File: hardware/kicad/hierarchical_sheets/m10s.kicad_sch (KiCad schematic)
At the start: 0 parts

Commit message: massive comment upload
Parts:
- added U7: MAX-M10S, RF_GPS:ublox_MAX, symbol RF_GPS:MAX-M10S
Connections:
- new net: U7.1 (GND), U7.10 (GND), U7.12 (GND)
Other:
- note added: "Comments: - The I2C address is 0x42 (pg 15 in datasheet). Put something like "Addr: 0x42" in a text label near the bottom right of the chip so we know for future reference. - Since we are using I2C, we do not need the UART pins. Mark RXD and TXD as no connect - RF_IN: This is the main antenna connection, connect it to the SMA connector that is in the parts library under the name "CONSMA020.062-G"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"
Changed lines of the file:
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@@
     (company "Missouri S&T Rocket Design Team")
   )
+  (text "Comments:\n\n- The I2C address is 0x42 (pg 15 in datasheet). Put something like \"Addr: 0x42\" in a text label near the bottom right\n	of the chip so we know for future reference. \n\n- Since we are using I2C, we do not need the UART pins. Mark RXD and TXD as no connect\n\n- RF_IN: This is the main antenna connection, connect it to the SMA connector that is in the parts library under the\n	 name \"CONSMA020.062-G\". Pin 2 of that sma connector is the shield and should just go to ground. \n\n- Page 11 of the daatasheet: both VCC and VCC_IO are the supply pins. Connect both of these to 3.3v. Since they are the main supply\n	pins put two 100n capacitors on the schematic between 3.3v and gnd. These are decoupling capacitors that need to be placed \n	near the chip on the pcb. To help us remember, place them physically close to the vcc pins on the schematic. Check the \n	microcontroller schematic for an example.\n\n- On page 28 of the M10s integration manual (I just added this to datasheets), it says to leave the V_BCKP pin disconnected \n	if a backup supply is not used. Thus put a no connect on the V_BCKP pin. \n\n- On page 6 of the M10s integration manual, it says that VCC_RF is an optional voltage output for powering an optional external\n	LNA or active antenna. Since we are using a passive antenna just put a no connect on the VCC_RF pin. \n\n- Since there is no external LNA mark the LNA_EN as disabled\n\n- The Timepulse pin can be used to output a very precise time signal (gps atomic clock precision). We don't need it so just \n	mark it as no connect\n\n- The ExtInt pin is a configurable interrupt. We don't really have the need or pins for this so just mark it as no connect. \n\n- SDA and SCL are the I2C data lines, connect them to hierarchical labels so that we can connect them to the microcontroller\n	outside this schematic\n\n- The safeboot pin is used for flashing the chip firmware. We do not need to do this (hopefully) so just mark it as no connect.\n	\n- The VIO_SEL selects the I/O voltage for the module. According to page 9 of the datasheet, this pin should be left open (unconnected)\n	for 3.3v logic levels. As such, mark this pin as no connect. \n\n- NOTE!!!: We need to check the max10s footprint, i briefly looked at it and i\n	thought all the pins were reveresed when comparing it to the datasheet.\n	Unsure if datasheet is not clear or if the kicad footprint is backwards\n\n			-Seth"
+    (at 179.705 161.925 0)
+    (effects (font (size 2 2) (thickness 0.4) bold (color 255 48 0 1)) (justify left bottom))
+  )
+  (symbol (lib_id "RF_GPS:MAX-M10S") (at 95.885 93.345 0) (unit 1)
+    (in_bom yes) (on_board yes) (dnp no) (fields_autoplaced)
+    (property "Reference" "U7" (at 98.0791 110.49 0)
+      (effects (font (size 1.27 1.27)) (justify left))
+    )
+    (property "Value" "MAX-M10S" (at 98.0791 113.03 0)
+      (effects (font (size 1.27 1.27)) (justify left))
+    )
+    (property "Footprint" "RF_GPS:ublox_MAX" (at 106.045 109.855 0)
+      (effects (font (size 1.27 1.27)) hide)
+    )
+    (property "Datasheet" "https://content.u-blox.com/sites/default/files/MAX-M10S_DataSheet_UBX-20035208.pdf" (at 95.885 93.345 0)
+      (effects (font (size 1.27 1.27)) hide)
+    )
+    (pin "1")
+    (pin "10")
+    (pin "11")
+    (pin "12")
+    (pin "13")
+    (pin "14")
+    (pin "15")
+    (pin "16")
+    (pin "17")
+    (pin "18")
+    (pin "2")
+    (pin "3")
+    (pin "4")
+    (pin "5")
+    (pin "6")
+    (pin "7")
+    (pin "8")
+    (pin "9")
+    (instances
+      (project "FC"
+        (path "/54cce219-8b98-4e71-96c4-f9ee784aa3bc/f2d155c9-a158-4cf0-b4ab-42b0987153ce"
+          (reference "U7") (unit 1)
+        )
+      )
+    )
+  )
 )

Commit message: made gps
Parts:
- added C1, C2: 100n, symbol Device:C_Small
- added J5: CONSMA020.062-G, CONSMA020.062:CONSMA020.062-G, symbol CONSMA020.062-G:CONSMA020.062-G
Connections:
- net GND: now reaches U7.1 (GND), U7.10 (GND), U7.12 (GND)
- net GND: now also C1.2, C2.2, J5.2 (Ext)
- net at U7.11 (RF_IN): now also J5.1 (In)
- net SDA: now reaches U7.16 (SDA)
- net ~{SCL}: now reaches U7.17 (SCL)
- net +3.3V: now reaches U7.7 (VCC_IO)
- net +3.3V: now also U7.8 (VCC), C1.1, C2.1
- no-connect marks 0 -> 10
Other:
- note added: "Addr: 0x42"
- note added: "max current: 15 mA"

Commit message: made gps
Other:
- note removed: "Comments: - The I2C address is 0x42 (pg 15 in datasheet). Put something like "Addr: 0x42" in a text label near the bottom right of the chip so we know for future reference. - Since we are using I2C, we do not need the UART pins. Mark RXD and TXD as no connect - RF_IN: This is the main antenna connection, connect it to the SMA connector that is in the parts library under the name "CONSMA020.062-G"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"
- moved on the sheet: C1, C2, J5, U7

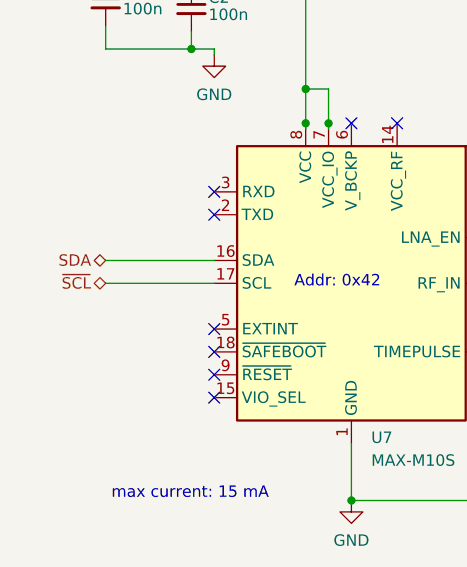
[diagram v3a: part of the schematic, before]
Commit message: corrected I2c line labels
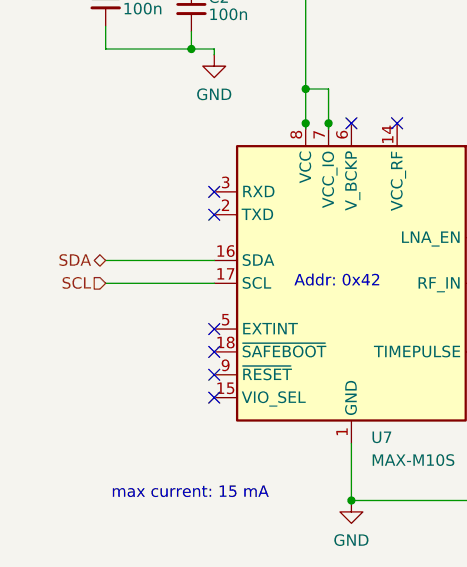
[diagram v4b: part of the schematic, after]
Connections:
- net ~{SCL} renamed SCL
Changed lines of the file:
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@@
     (effects (font (size 1.27 1.27)) (justify left bottom))
   )
-  (hierarchical_label "~{SCL}" (shape bidirectional) (at 111.76 94.615 180) (fields_autoplaced)
+  (hierarchical_label "SCL" (shape input) (at 111.76 94.615 180) (fields_autoplaced)
     (effects (font (size 1.27 1.27)) (justify right))
   )
